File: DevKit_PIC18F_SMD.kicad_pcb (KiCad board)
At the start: 2 copper layers, 27 x 53.5 mm, 25 parts, among them J1 PIC_ICSP_ICD, J2 USB_B_Mini, J5 RIGHT_PORT, J6 LEFT_PORT, SW1 C318938, X1 16MHz

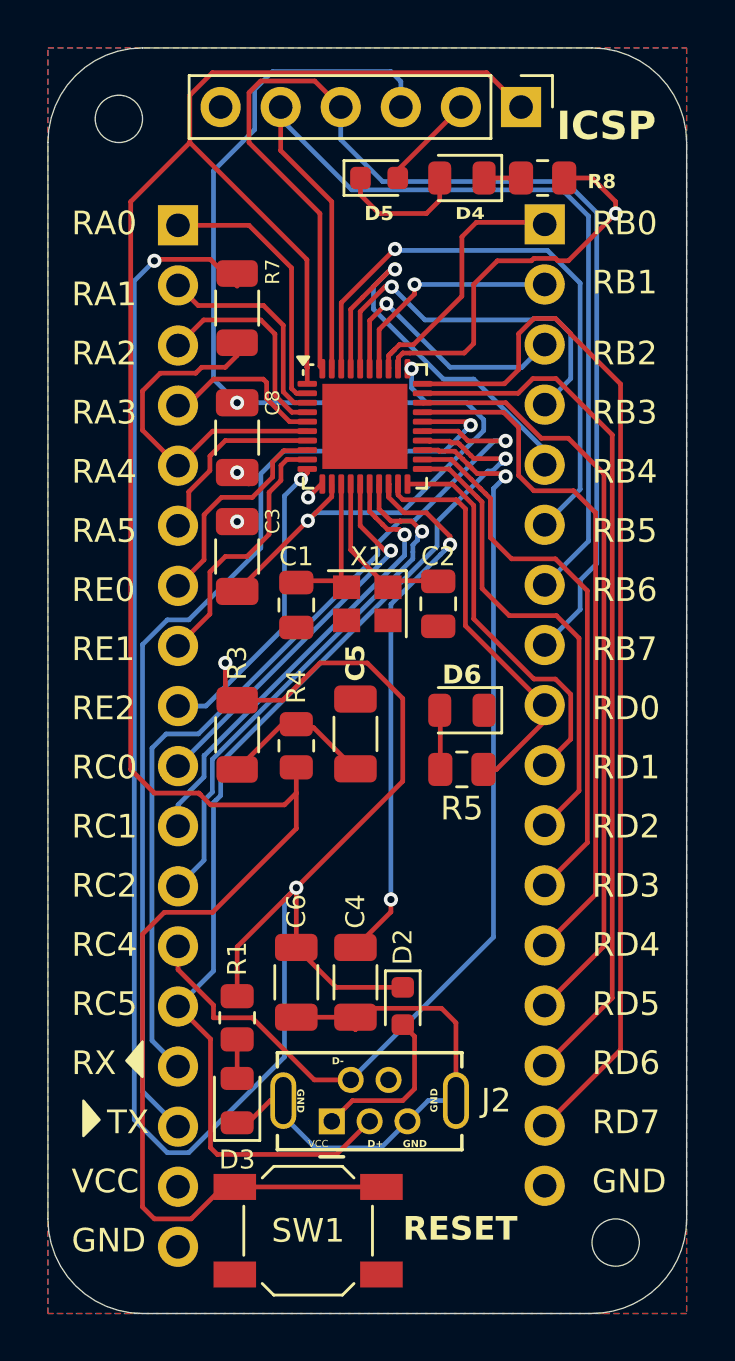
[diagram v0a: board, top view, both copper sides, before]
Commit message: Fix Reset Button, ICSP... etc.
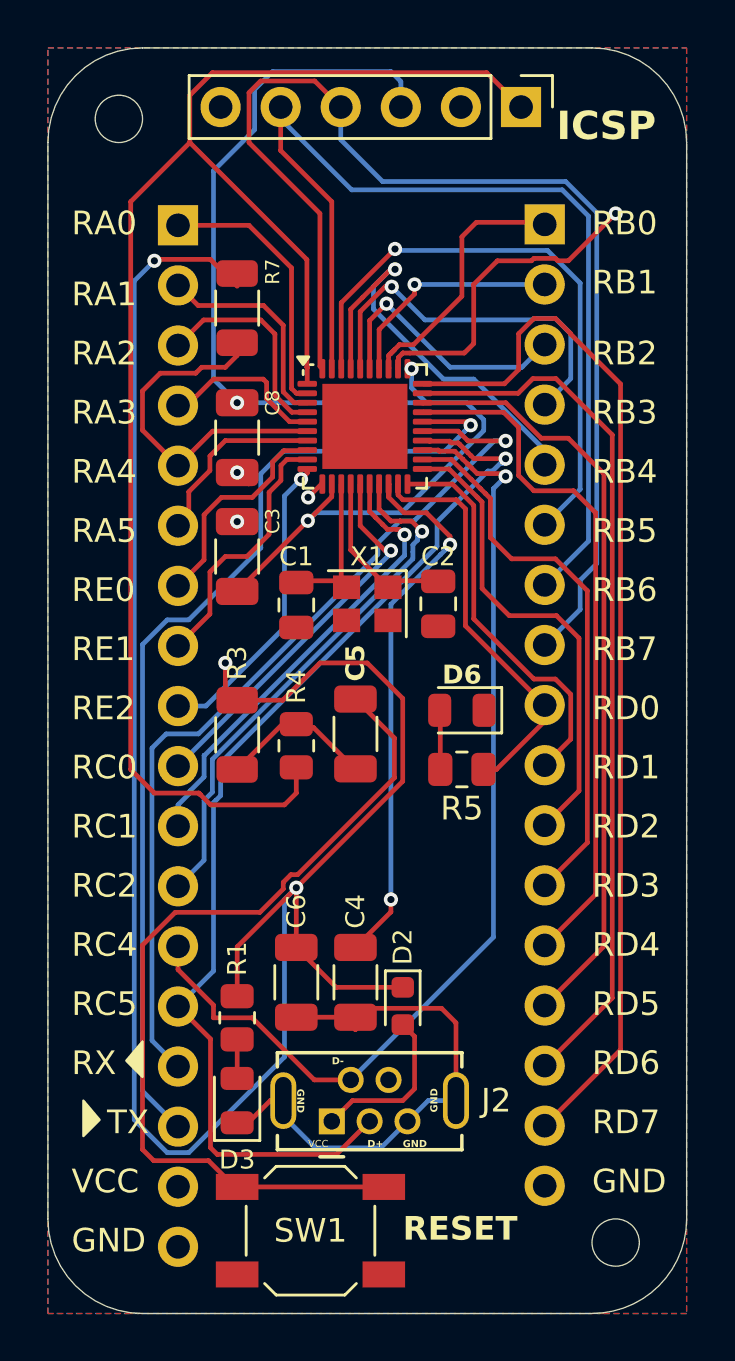
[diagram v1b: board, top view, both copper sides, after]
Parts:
- removed D4: LED_ICSP, LED_SMD:LED_0805_2012Metric
- removed D5: D_Schottky, Diode_SMD:D_0603_1608Metric
- removed R8: 470, Resistor_SMD:R_0805_2012Metric
- moved SW1 0.10 mm to (83.1, 76.5)
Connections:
- C5 pad 1: GND -> Net-(C5-Pad1)
- J1 pad 2: Net-(D5-A) -> VCC
- SW1 pad 1: /MCLR -> Net-(C5-Pad1)
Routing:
- net Net-(C5-Pad1): track 0.00 -> 37.6 mm
- net /MCLR: track 98.0 -> 65.7 mm
- net Net-(D4-A): track 5.56 -> 0.00 mm
- net Net-(D5-A): track 4.61 -> 0.00 mm
- net VCC: track 108.2 -> 105.6 mm
- net Net-(D4-K): track 1.56 -> 0.00 mm
